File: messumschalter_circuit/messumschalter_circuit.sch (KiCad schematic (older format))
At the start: 1 part

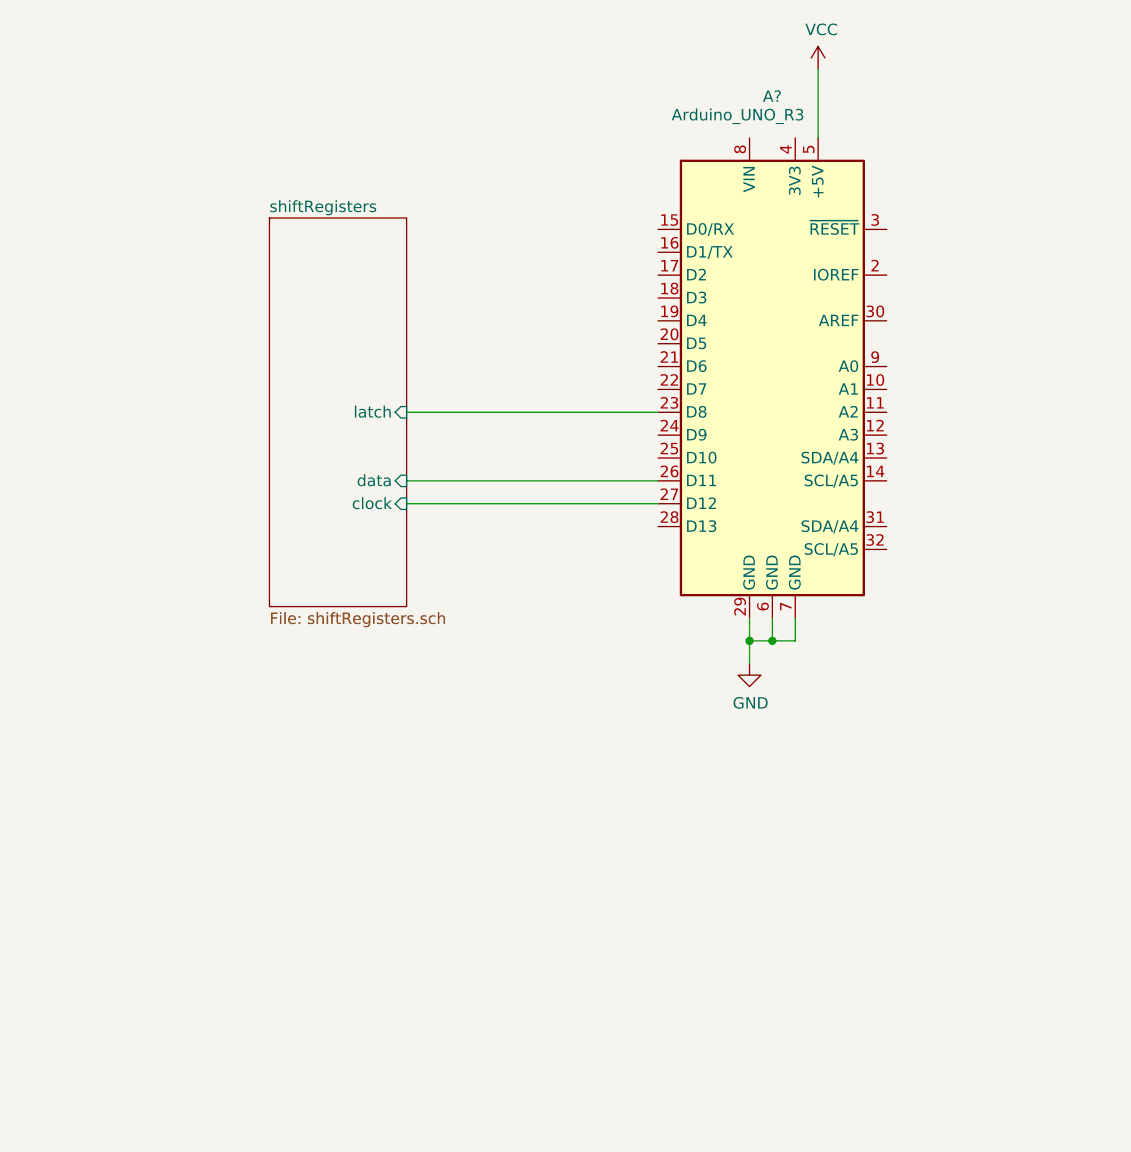
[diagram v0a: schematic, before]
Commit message: reduce to double 595 per board, leds and dip
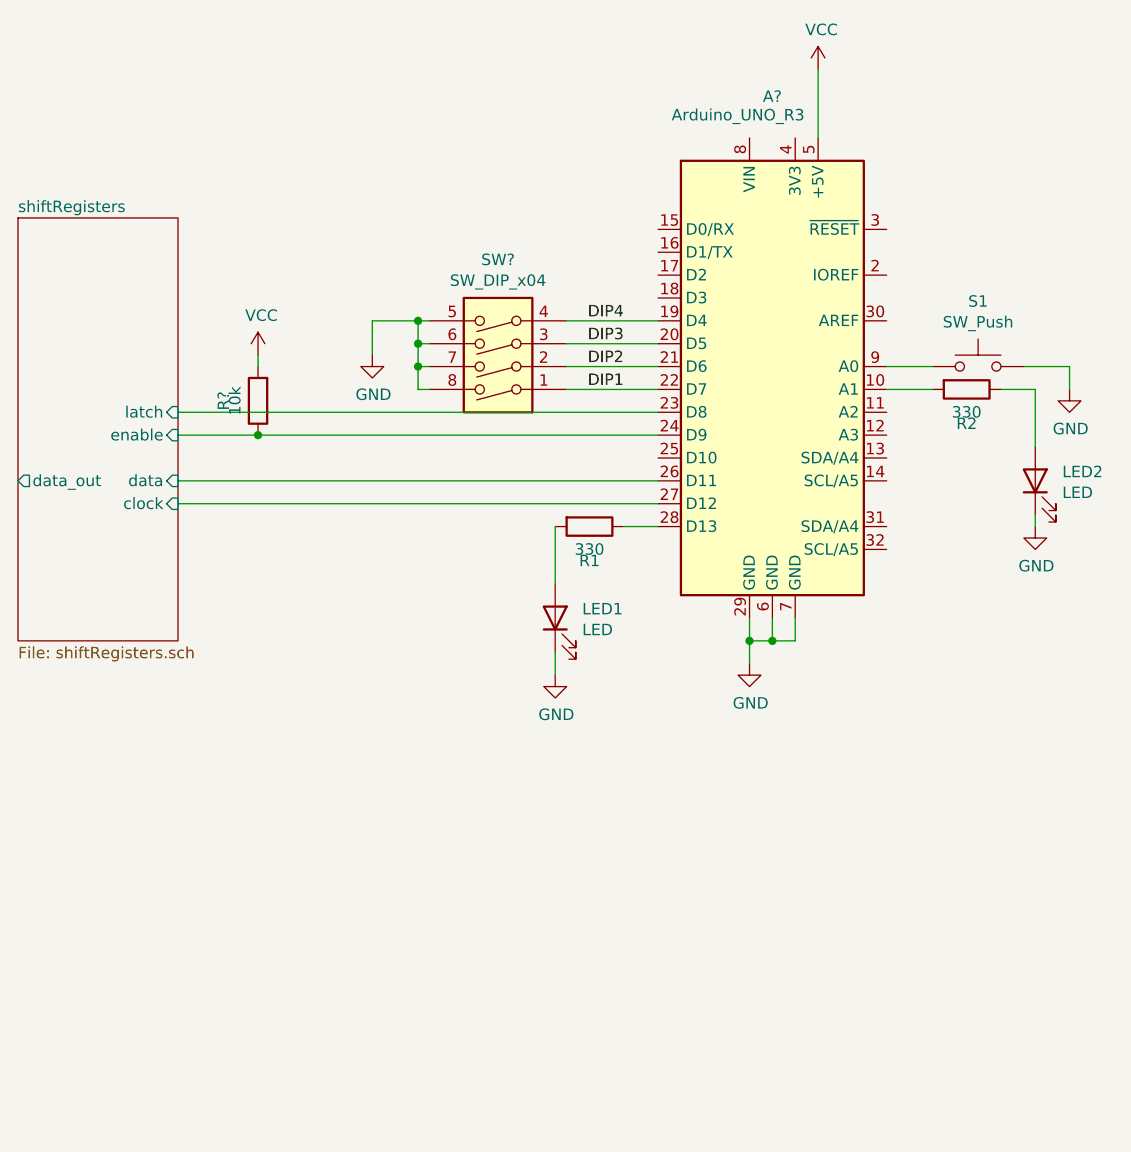
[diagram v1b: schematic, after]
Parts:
- added LED1, LED2: LED, symbol Device:LED
- added R1, R2: 330, symbol Device:R
- added R?: 10k, symbol Device:R
- added S1: SW_Push, symbol Switch:SW_Push
- added SW?: SW_DIP_x04, symbol Switch:SW_DIP_x04
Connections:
- net GND: now also LED1.1 (K), LED2.1 (K), S1.2, SW?.5, SW?.6, SW?.7, SW?.8
- net VCC: now also R?.2
- net at A?.10 (A1): now also R2.2
- net DIP4: now reaches A?.19 (D4)
- net DIP4: now also SW?.4
- net DIP3: now reaches A?.20 (D5)
- net DIP3: now also SW?.3
- net DIP2: now reaches A?.21 (D6)
- net DIP2: now also SW?.2
- net DIP1: now reaches A?.22 (D7)
- net DIP1: now also SW?.1
- net shiftRegisters/enable: now reaches A?.24 (D9)
- net shiftRegisters/enable: now also R?.1
- net at A?.28 (D13): now also R1.1
- net at A?.9 (A0): now also S1.1
- new net: LED1.2 (A), R1.2
- new net: LED2.2 (A), R2.1
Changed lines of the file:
@@
 	5550 3400 5550 3300
 Connection ~ 5450 3400
+Wire Wire Line
+	4950 2800 2850 2800
+Wire Wire Line
+	2850 2700 4950 2700
+Wire Wire Line
+	5650 1200 5650 900
+$Comp
+L Switch:SW_DIP_x04 SW?
+U 1 1 5F9A2CE5
+P 4250 2100
+F 0 "SW?" H 4250 1733 50  0000 C CNN
+F 1 "SW_DIP_x04" H 4250 1824 50  0000 C CNN
+F 2 "" H 4250 2100 50  0001 C CNN
+F 3 "~" H 4250 2100 50  0001 C CNN
+	1    4250 2100
+	-1   0    0    1
+$EndComp
+$Comp
+L Switch:SW_Push S1
+U 1 1 5F9A3E51
+P 6350 2200
+F 0 "S1" H 6350 2485 50  0000 C CNN
+F 1 "SW_Push" H 6350 2394 50  0000 C CNN
+F 2 "" H 6350 2400 50  0001 C CNN
+F 3 "~" H 6350 2400 50  0001 C CNN
+	1    6350 2200
+	1    0    0    -1
+$EndComp
+Wire Wire Line
+	6150 2200 5950 2200
+$Comp
+L power:GND #PWR?
+U 1 1 5F9A50E1
+P 6750 2300
+F 0 "#PWR?" H 6750 2050 50  0001 C CNN
+F 1 "GND" H 6755 2127 50  0000 C CNN
+F 2 "" H 6750 2300 50  0001 C CNN
+F 3 "" H 6750 2300 50  0001 C CNN
+	1    6750 2300
+	1    0    0    -1
+$EndComp
+Wire Wire Line
+	6750 2300 6750 2200
+Wire Wire Line
+	6750 2200 6550 2200
+$Comp
+L Device:LED LED1
+U 1 1 5F9A5A2B
+P 4500 3300
+F 0 "LED1" V 4539 3182 50  0000 R CNN
+F 1 "LED" V 4448 3182 50  0000 R CNN
+F 2 "" H 4500 3300 50  0001 C CNN
+F 3 "~" H 4500 3300 50  0001 C CNN
+	1    4500 3300
+	0    -1   -1   0
+$EndComp
+$Comp
+L power:GND #PWR?
+U 1 1 5F9A7E48
+P 4500 3550
+F 0 "#PWR?" H 4500 3300 50  0001 C CNN
+F 1 "GND" H 4505 3377 50  0000 C CNN
+F 2 "" H 4500 3550 50  0001 C CNN
+F 3 "" H 4500 3550 50  0001 C CNN
+	1    4500 3550
+	1    0    0    -1
+$EndComp
+Wire Wire Line
+	4500 3550 4500 3450
+$Comp
+L Device:R R1
+U 1 1 5F9A8586
+P 4650 2900
+F 0 "R1" V 4800 2900 50  0000 C CNN
+F 1 "330" V 4750 2900 50  0000 C CNN
+F 2 "" V 4580 2900 50  0001 C CNN
+F 3 "~" H 4650 2900 50  0001 C CNN
+	1    4650 2900
+	0    1    1    0
+$EndComp
+Wire Wire Line
+	4950 2900 4800 2900
+Wire Wire Line
+	4500 2900 4500 3150
+Wire Wire Line
+	2850 2500 3200 2500
+$Comp
+L Device:R R?
+U 1 1 5FA55527
+P 3200 2350
+F 0 "R?" V 3350 2350 50  0000 C CNN
+F 1 "10k" V 3300 2350 50  0000 C CNN
+F 2 "" V 3130 2350 50  0001 C CNN
+F 3 "~" H 3200 2350 50  0001 C CNN
+	1    3200 2350
+	-1   0    0    1
+$EndComp
+Connection ~ 3200 2500
+$Comp
+L power:VCC #PWR?
+U 1 1 5FA5A746
+P 3200 2150
+F 0 "#PWR?" H 3200 2000 50  0001 C CNN
+F 1 "VCC" H 3215 2323 50  0000 C CNN
+F 2 "" H 3200 2150 50  0001 C CNN
+F 3 "" H 3200 2150 50  0001 C CNN
+	1    3200 2150
+	1    0    0    -1
+$EndComp
+Wire Wire Line
+	3200 2200 3200 2150
 $Sheet
-S 3250 1550 600  1700
+S 2150 1550 700  1850
 U 5F8E5C53
 F0 "shiftRegisters" 50
 F1 "shiftRegisters.sch" 50
-F2 "latch" I R 3850 2400 50
-F3 "clock" I R 3850 2800 50
-F4 "data" I R 3850 2700 50
+F2 "latch" I R 2850 2400 50
+F3 "clock" I R 2850 2800 50
+F4 "data" I R 2850 2700 50
+F5 "data_out" O L 2150 2700 50
+F6 "enable" I R 2850 2500 50
 $EndSheet
 Wire Wire Line
-	4950 2800 3850 2800
-Wire Wire Line
-	3850 2700 4950 2700
-Wire Wire Line
-	4950 2400 3850 2400
-Wire Wire Line
-	5650 1200 5650 900
+	2850 2400 4950 2400
+Wire Wire Line
+	3200 2500 4950 2500
+Wire Wire Line
+	4550 2300 4950 2300
+Wire Wire Line
+	4950 2200 4550 2200
+Wire Wire Line
+	4550 2100 4950 2100
+Wire Wire Line
+	4950 2000 4550 2000
+Text Label 4800 2300 2    50   ~ 0
+DIP1
+Text Label 4800 2200 2    50   ~ 0
+DIP2
+Text Label 4800 2100 2    50   ~ 0
+DIP3
+Text Label 4800 2000 2    50   ~ 0
+DIP4
+$Comp
+L power:GND #PWR?
+U 1 1 5FA72551
+P 3700 2150
+F 0 "#PWR?" H 3700 1900 50  0001 C CNN
+F 1 "GND" H 3705 1977 50  0000 C CNN
+F 2 "" H 3700 2150 50  0001 C CNN
+F 3 "" H 3700 2150 50  0001 C CNN
+	1    3700 2150
+	1    0    0    -1
+$EndComp
+Wire Wire Line
+	3950 2300 3900 2300
+Wire Wire Line
+	3900 2300 3900 2200
+Wire Wire Line
+	3900 2000 3950 2000
+Wire Wire Line
+	3950 2100 3900 2100
+Connection ~ 3900 2100
+Wire Wire Line
+	3900 2100 3900 2000
+Wire Wire Line
+	3950 2200 3900 2200
+Connection ~ 3900 2200
+Wire Wire Line
+	3900 2200 3900 2100
+Wire Wire Line
+	3900 2000 3700 2000
+Wire Wire Line
+	3700 2000 3700 2150
+Connection ~ 3900 2000
+$Comp
+L Device:LED LED2
+U 1 1 5FA749A0
+P 6600 2700
+F 0 "LED2" V 6639 2582 50  0000 R CNN
+F 1 "LED" V 6548 2582 50  0000 R CNN
+F 2 "" H 6600 2700 50  0001 C CNN
+F 3 "~" H 6600 2700 50  0001 C CNN
+	1    6600 2700
+	0    -1   -1   0
+$EndComp
+$Comp
+L Device:R R2
+U 1 1 5FA74F35
+P 6300 2300
+F 0 "R2" V 6450 2300 50  0000 C CNN
+F 1 "330" V 6400 2300 50  0000 C CNN
+F 2 "" V 6230 2300 50  0001 C CNN
+F 3 "~" H 6300 2300 50  0001 C CNN
+	1    6300 2300
+	0    1    1    0
+$EndComp
+Wire Wire Line
+	5950 2300 6150 2300
+Wire Wire Line
+	6450 2300 6600 2300
+Wire Wire Line
+	6600 2300 6600 2550
+$Comp
+L power:GND #PWR?
+U 1 1 5FA796DE
+P 6600 2900
+F 0 "#PWR?" H 6600 2650 50  0001 C CNN
+F 1 "GND" H 6605 2727 50  0000 C CNN
+F 2 "" H 6600 2900 50  0001 C CNN
+F 3 "" H 6600 2900 50  0001 C CNN
+	1    6600 2900
+	1    0    0    -1
+$EndComp
+Wire Wire Line
+	6600 2900 6600 2850
 $EndSCHEMATC

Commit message: add second 595 board
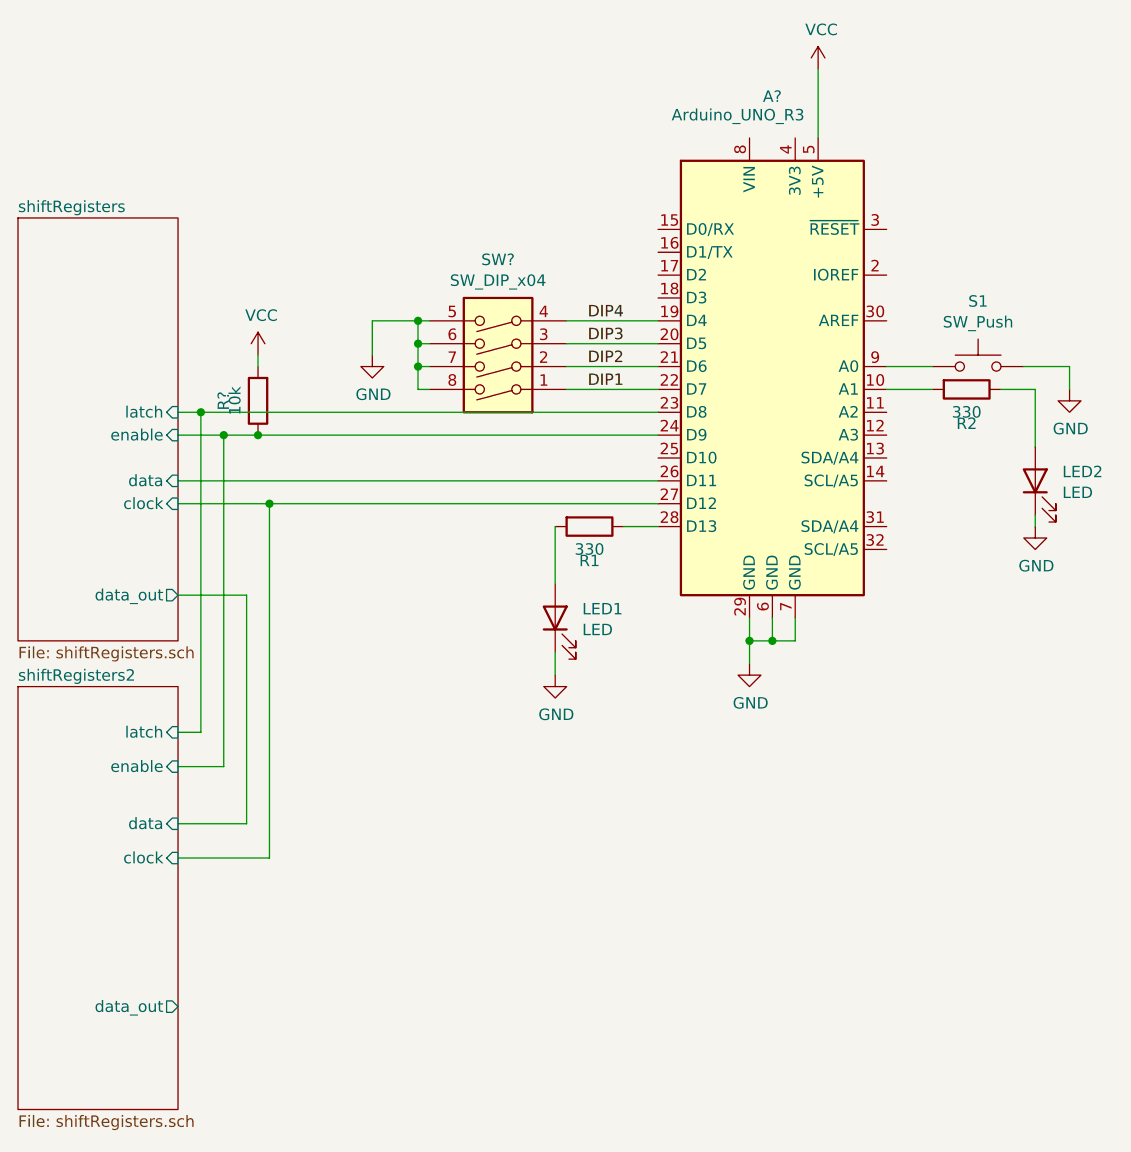
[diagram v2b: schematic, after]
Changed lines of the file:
@@
 $Descr A4 11693 8268
 encoding utf-8
-Sheet 1 2
+Sheet 1 3
 Title ""
 Date ""
@@
 Connection ~ 5450 3400
 Wire Wire Line
-	4950 2800 2850 2800
-Wire Wire Line
-	2850 2700 4950 2700
+	4950 2800 3250 2800
 Wire Wire Line
 	5650 1200 5650 900
@@
 	4500 2900 4500 3150
 Wire Wire Line
-	2850 2500 3200 2500
+	2850 2500 3050 2500
 $Comp
 L Device:R R?
@@
 Wire Wire Line
 	3200 2200 3200 2150
-$Sheet
-S 2150 1550 700  1850
-U 5F8E5C53
-F0 "shiftRegisters" 50
-F1 "shiftRegisters.sch" 50
-F2 "latch" I R 2850 2400 50
-F3 "clock" I R 2850 2800 50
-F4 "data" I R 2850 2700 50
-F5 "data_out" O L 2150 2700 50
-F6 "enable" I R 2850 2500 50
-$EndSheet
-Wire Wire Line
-	2850 2400 4950 2400
+Wire Wire Line
+	2850 2400 2950 2400
 Wire Wire Line
 	3200 2500 4950 2500
@@
 Wire Wire Line
 	6600 2900 6600 2850
+$Sheet
+S 2150 3600 700  1850
+U 5FA7BAF1
+F0 "shiftRegisters2" 50
+F1 "shiftRegisters.sch" 50
+F2 "latch" I R 2850 3800 50
+F3 "clock" I R 2850 4350 50
+F4 "data" I R 2850 4200 50
+F5 "data_out" O R 2850 5000 50
+F6 "enable" I R 2850 3950 50
+$EndSheet
+Wire Wire Line
+	2950 2400 2950 3800
+Wire Wire Line
+	2950 3800 2850 3800
+Connection ~ 2950 2400
+Wire Wire Line
+	2950 2400 4950 2400
+Wire Wire Line
+	3050 2500 3050 3950
+Wire Wire Line
+	3050 3950 2850 3950
+Connection ~ 3050 2500
+Wire Wire Line
+	3050 2500 3200 2500
+Wire Wire Line
+	3150 4200 2850 4200
+Wire Wire Line
+	3250 2800 3250 4350
+Wire Wire Line
+	3250 4350 2850 4350
+Connection ~ 3250 2800
+Wire Wire Line
+	3250 2800 2850 2800
+Wire Wire Line
+	2850 2700 4950 2700
+Wire Wire Line
+	2850 3200 3150 3200
+Wire Wire Line
+	3150 3200 3150 4200
+$Sheet
+S 2150 1550 700  1850
+U 5F8E5C53
+F0 "shiftRegisters" 50
+F1 "shiftRegisters.sch" 50
+F2 "latch" I R 2850 2400 50
+F3 "clock" I R 2850 2800 50
+F4 "data" I R 2850 2700 50
+F5 "data_out" O R 2850 3200 50
+F6 "enable" I R 2850 2500 50
+$EndSheet
 $EndSCHEMATC
